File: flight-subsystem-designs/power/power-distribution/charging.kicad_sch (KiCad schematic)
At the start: 10 parts, among them U14 LTM8062AIV-PBF

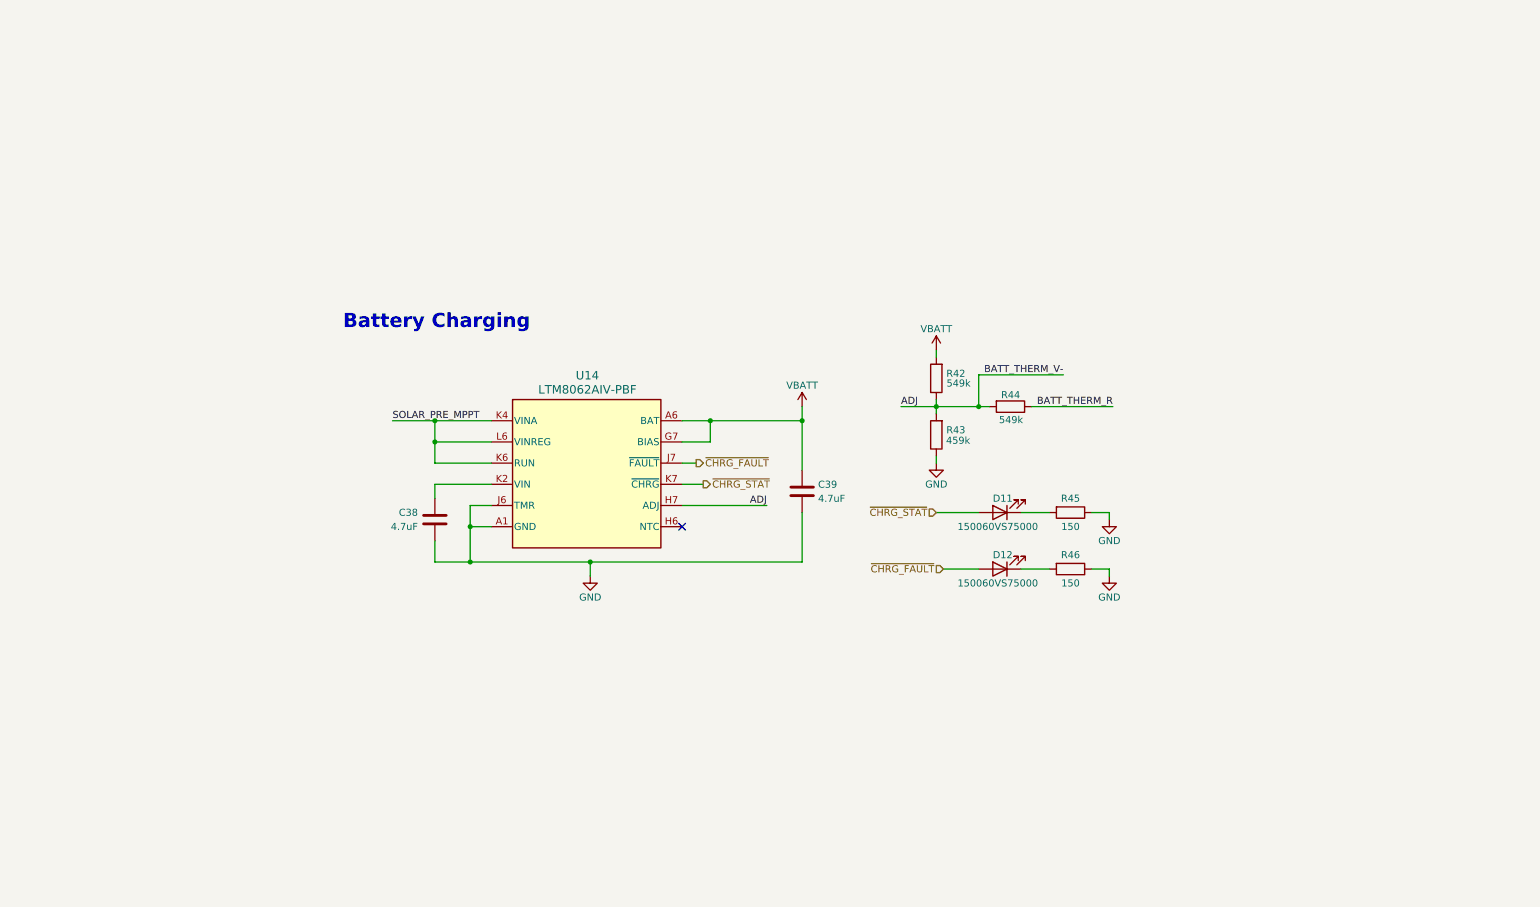
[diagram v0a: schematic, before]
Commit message: feat: PDU 4.0.0 (WIP)
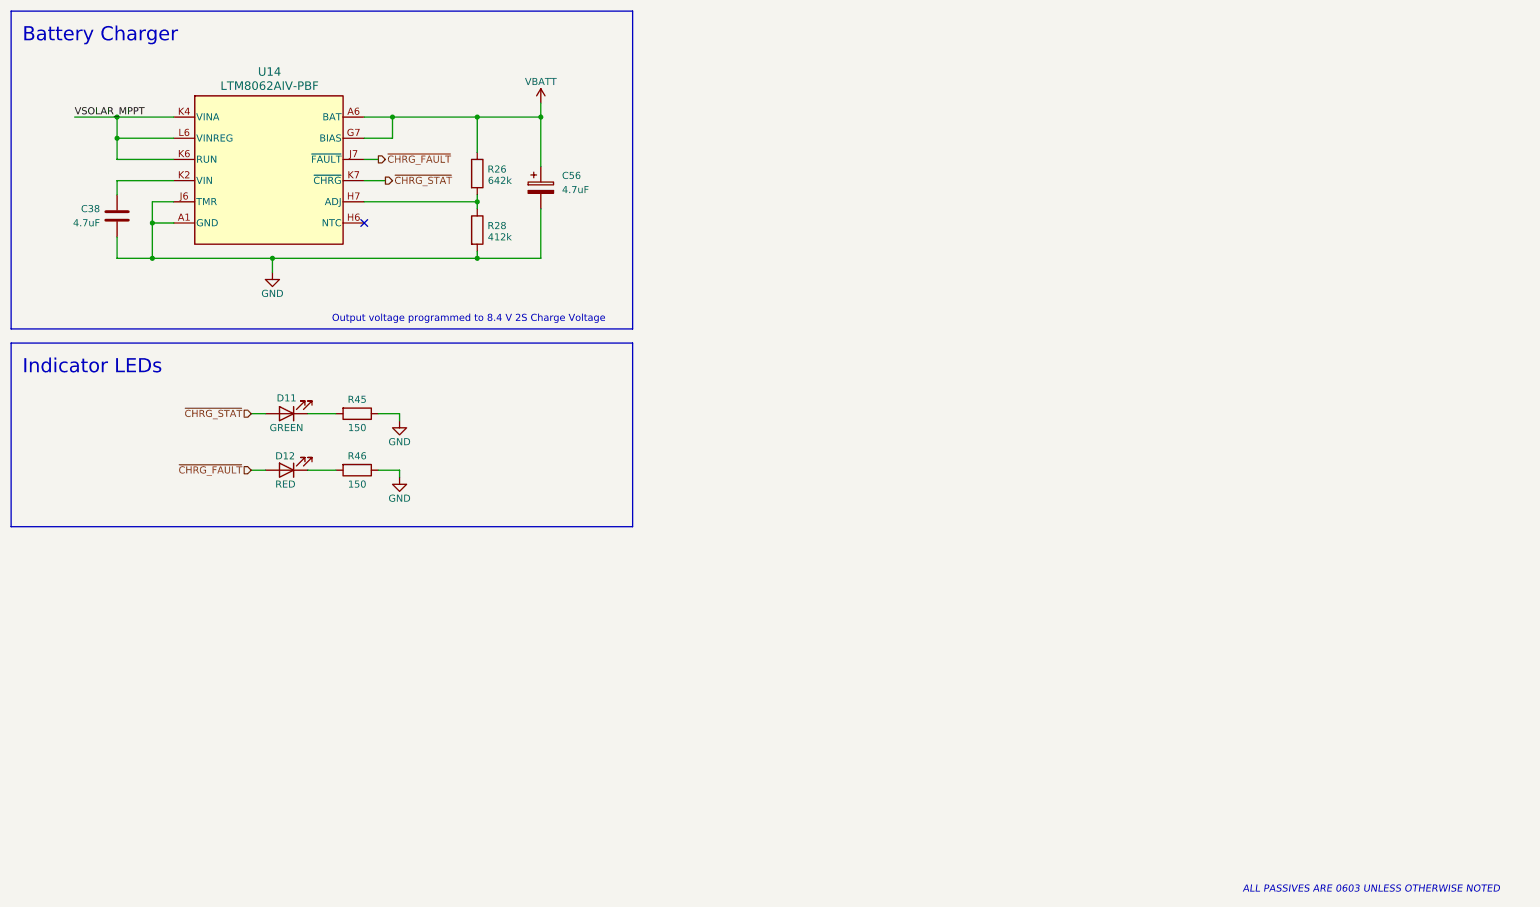
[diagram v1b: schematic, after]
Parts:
- removed C39: 4.7uF, Capacitor_Tantalum_SMD:CP_EIA-3528-12_Kemet-T, symbol Device:C
- removed R42, R44: 549k, Resistor_SMD:R_0603_1608Metric, symbol Device:R
- removed R43: 459k, Resistor_SMD:R_0603_1608Metric, symbol Device:R
- added C56: 4.7uF, Capacitor_Tantalum_SMD:CP_EIA-3528-12_Kemet-T, symbol Device:C_Polarized
- added R26: 642k, Resistor_SMD:R_0603_1608Metric, symbol Device:R
- added R28: 412k, Resistor_SMD:R_0603_1608Metric, symbol Device:R
- D11: value 150060VS75000 -> GREEN
- D12: value 150060VS75000 -> RED
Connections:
- net GND: now also C56.2, R28.2
- net VBATT: now also C56.1, R26.1
- net ADJ: no longer names the net of U14.H7 (ADJ)
- net ADJ: now also R26.2, R28.1
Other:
- note added: "ALL PASSIVES ARE 0603 UNLESS OTHERWISE NOTED"
- note added: "Battery Charger"
- note added: "Indicator LEDs"
- note added: "Output voltage programmed to 8.4 V 2S Charge Voltage"
- note removed: "Battery Charging"
- moved on the sheet: C38, D11, D12, R45, R46, U14

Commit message: shi
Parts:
- renumbered C38 to C2, C56 to C3, R45 to R1, R46 to R2
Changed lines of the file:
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@@
-	)
-	(junction
-		(at 33.02 33.02)
-		(diameter 0)
-		(color 0 0 0 0)
 	)
 	(junction
@@
 	)
 	(junction
+		(at 39.37 36.83)
+		(diameter 0)
+		(color 0 0 0 0)
+	)
+	(junction
+		(at 39.37 33.02)
+		(diameter 0)
+		(color 0 0 0 0)
+	)
+	(junction
 		(at 60.96 58.42)
 		(diameter 0)
@@
 	)
 	(junction
-		(at 33.02 36.83)
-		(diameter 0)
-		(color 0 0 0 0)
-	)
-	(junction
 		(at 39.37 52.07)
 		(diameter 0)
@@
 	(wire
 		(pts
-			(xy 43.18 40.64) (xy 33.02 40.64)
+			(xy 43.18 40.64) (xy 39.37 40.64)
 		)
 		(stroke
@@
 	(wire
 		(pts
+			(xy 39.37 36.83) (xy 43.18 36.83)
+		)
+		(stroke
+			(width 0)
+			(type default)
+		)
+	)
+	(wire
+		(pts
+			(xy 36.83 33.02) (xy 39.37 33.02)
+		)
+		(stroke
+			(width 0)
+			(type default)
+		)
+	)
+	(wire
+		(pts
 			(xy 43.18 52.07) (xy 39.37 52.07)
 		)
@@
 	(wire
 		(pts
-			(xy 33.02 36.83) (xy 43.18 36.83)
-		)
-		(stroke
-			(width 0)
-			(type default)
-		)
-	)
-	(wire
-		(pts
 			(xy 77.47 36.83) (xy 82.55 36.83)
 		)
@@
 	(wire
 		(pts
-			(xy 33.02 40.64) (xy 33.02 36.83)
+			(xy 39.37 40.64) (xy 39.37 36.83)
 		)
 		(stroke
@@
 	(wire
 		(pts
-			(xy 33.02 33.02) (xy 43.18 33.02)
-		)
-		(stroke
-			(width 0)
-			(type default)
-		)
-	)
-	(wire
-		(pts
 			(xy 72.39 96.52) (xy 67.31 96.52)
 		)
@@
 	(wire
 		(pts
-			(xy 25.4 33.02) (xy 33.02 33.02)
+			(xy 39.37 33.02) (xy 43.18 33.02)
 		)
 		(stroke
@@
 	(wire
 		(pts
-			(xy 33.02 36.83) (xy 33.02 33.02)
+			(xy 39.37 36.83) (xy 39.37 33.02)
 		)
 		(stroke
@@
 			(width 0)
 			(type default)
-		)
-	)
-	(label "VSOLAR_MPPT"
-		(at 25.4 33.02 0)
-		(effects
-			(font
-				(size 1.27 1.27)
-			)
-			(justify left bottom)
 		)
 	)
@@
 			)
 			(justify left)
+		)
+	)
+	(hierarchical_label "VSOLAR_MPPT"
+		(shape bidirectional)
+		(at 36.83 33.02 180)
+		(effects
+			(font
+				(size 1.27 1.27)
+			)
+			(justify right)
 		)
 	)
@@
 		(instances
 			(project "PowerDistribution"
-				(path "/7c5a015a-5b4f-4b5c-9bf9-4b89ce9a73a3/e5a3dfcb-cd7b-4560-b476-c806ed59e5ac"
+				(path "/7c5a015a-5b4f-4b5c-9bf9-4b89ce9a73a3/3e64ef40-6854-4352-ae82-05e7be8eedfd"
 					(reference "R26")
 					(unit 1)
@@
 		(on_board yes)
 		(dnp no)
-		(property "Reference" "R45"
+		(property "Reference" "R1"
 			(at 76.2 83.82 90)
 			(effects
@@
 		(instances
 			(project "PowerDistribution"
-				(path "/7c5a015a-5b4f-4b5c-9bf9-4b89ce9a73a3/e5a3dfcb-cd7b-4560-b476-c806ed59e5ac"
-					(reference "R45")
+				(path "/7c5a015a-5b4f-4b5c-9bf9-4b89ce9a73a3/3e64ef40-6854-4352-ae82-05e7be8eedfd"
+					(reference "R1")
 					(unit 1)
 				)
@@
 		(on_board yes)
 		(dnp no)
-		(property "Reference" "C38"
+		(property "Reference" "C2"
 			(at 29.972 49.53 0)
 			(effects
@@
 		(instances
 			(project "PowerDistribution"
-				(path "/7c5a015a-5b4f-4b5c-9bf9-4b89ce9a73a3/e5a3dfcb-cd7b-4560-b476-c806ed59e5ac"
-					(reference "C38")
+				(path "/7c5a015a-5b4f-4b5c-9bf9-4b89ce9a73a3/3e64ef40-6854-4352-ae82-05e7be8eedfd"
+					(reference "C2")
 					(unit 1)
 				)
@@
 		(instances
 			(project "PowerDistribution"
-				(path "/7c5a015a-5b4f-4b5c-9bf9-4b89ce9a73a3/e5a3dfcb-cd7b-4560-b476-c806ed59e5ac"
+				(path "/7c5a015a-5b4f-4b5c-9bf9-4b89ce9a73a3/3e64ef40-6854-4352-ae82-05e7be8eedfd"
 					(reference "D12")
 					(unit 1)
@@
 		(on_board yes)
 		(dnp no)
-		(property "Reference" "#PWR064"
+		(property "Reference" "#PWR010"
 			(at 109.22 34.29 0)
 			(effects
@@
 		(instances
 			(project "PowerDistribution"
-				(path "/7c5a015a-5b4f-4b5c-9bf9-4b89ce9a73a3/e5a3dfcb-cd7b-4560-b476-c806ed59e5ac"
-					(reference "#PWR064")
+				(path "/7c5a015a-5b4f-4b5c-9bf9-4b89ce9a73a3/3e64ef40-6854-4352-ae82-05e7be8eedfd"
+					(reference "#PWR010")
 					(unit 1)
 				)
@@
 		(on_board yes)
 		(dnp no)
-		(property "Reference" "#PWR072"
+		(property "Reference" "#PWR03"
 			(at 83.82 104.14 0)
 			(effects
@@
 		(instances
 			(project "PowerDistribution"
-				(path "/7c5a015a-5b4f-4b5c-9bf9-4b89ce9a73a3/e5a3dfcb-cd7b-4560-b476-c806ed59e5ac"
-					(reference "#PWR072")
+				(path "/7c5a015a-5b4f-4b5c-9bf9-4b89ce9a73a3/3e64ef40-6854-4352-ae82-05e7be8eedfd"
+					(reference "#PWR03")
 					(unit 1)
 				)
@@
 		(dnp no)
 		(fields_autoplaced yes)
-		(property "Reference" "C56"
+		(property "Reference" "C3"
 			(at 113.03 43.5609 0)
 			(effects
@@
 		)
 		(instances
-			(project ""
-				(path "/7c5a015a-5b4f-4b5c-9bf9-4b89ce9a73a3/e5a3dfcb-cd7b-4560-b476-c806ed59e5ac"
-					(reference "C56")
+			(project "PowerDistribution"
+				(path "/7c5a015a-5b4f-4b5c-9bf9-4b89ce9a73a3/3e64ef40-6854-4352-ae82-05e7be8eedfd"
+					(reference "C3")
 					(unit 1)
 				)
@@
 		(instances
 			(project "PowerDistribution"
-				(path "/7c5a015a-5b4f-4b5c-9bf9-4b89ce9a73a3/e5a3dfcb-cd7b-4560-b476-c806ed59e5ac"
+				(path "/7c5a015a-5b4f-4b5c-9bf9-4b89ce9a73a3/3e64ef40-6854-4352-ae82-05e7be8eedfd"
 					(reference "R28")
 					(unit 1)
@@
 		(instances
 			(project "PowerDistribution"
-				(path "/7c5a015a-5b4f-4b5c-9bf9-4b89ce9a73a3/e5a3dfcb-cd7b-4560-b476-c806ed59e5ac"
+				(path "/7c5a015a-5b4f-4b5c-9bf9-4b89ce9a73a3/3e64ef40-6854-4352-ae82-05e7be8eedfd"
 					(reference "U14")
 					(unit 1)
@@
 		(instances
 			(project "PowerDistribution"
-				(path "/7c5a015a-5b4f-4b5c-9bf9-4b89ce9a73a3/e5a3dfcb-cd7b-4560-b476-c806ed59e5ac"
+				(path "/7c5a015a-5b4f-4b5c-9bf9-4b89ce9a73a3/3e64ef40-6854-4352-ae82-05e7be8eedfd"
 					(reference "D11")
 					(unit 1)
@@
 		(on_board yes)
 		(dnp no)
-		(property "Reference" "#PWR061"
+		(property "Reference" "#PWR01"
 			(at 60.96 67.31 0)
 			(effects
@@
 		(instances
 			(project "PowerDistribution"
-				(path "/7c5a015a-5b4f-4b5c-9bf9-4b89ce9a73a3/e5a3dfcb-cd7b-4560-b476-c806ed59e5ac"
-					(reference "#PWR061")
+				(path "/7c5a015a-5b4f-4b5c-9bf9-4b89ce9a73a3/3e64ef40-6854-4352-ae82-05e7be8eedfd"
+					(reference "#PWR01")
 					(unit 1)
 				)
@@
 		(on_board yes)
 		(dnp no)
-		(property "Reference" "R46"
+		(property "Reference" "R2"
 			(at 76.2 93.98 90)
 			(effects
@@
 		(instances
 			(project "PowerDistribution"
-				(path "/7c5a015a-5b4f-4b5c-9bf9-4b89ce9a73a3/e5a3dfcb-cd7b-4560-b476-c806ed59e5ac"
-					(reference "R46")
+				(path "/7c5a015a-5b4f-4b5c-9bf9-4b89ce9a73a3/3e64ef40-6854-4352-ae82-05e7be8eedfd"
+					(reference "R2")
 					(unit 1)
 				)
@@
 		(on_board yes)
 		(dnp no)
-		(property "Reference" "#PWR071"
+		(property "Reference" "#PWR02"
 			(at 83.82 93.98 0)
 			(effects
@@
 		(instances
 			(project "PowerDistribution"
-				(path "/7c5a015a-5b4f-4b5c-9bf9-4b89ce9a73a3/e5a3dfcb-cd7b-4560-b476-c806ed59e5ac"
-					(reference "#PWR071")
+				(path "/7c5a015a-5b4f-4b5c-9bf9-4b89ce9a73a3/3e64ef40-6854-4352-ae82-05e7be8eedfd"
+					(reference "#PWR02")
 					(unit 1)
 				)
